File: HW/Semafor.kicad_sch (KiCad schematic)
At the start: 65 parts, among them J1 USB_C_Receptacle_USB2.0, J2 USB_plug, M1 Motor_DC, Q3 Q_NMOS_GSD, Q4 Q_NMOS_GSD, SW6 SW_SPDT, U1 ESP32-C3, U2 CN3058E, U3 LT1930, U4 E22-900T22D, U5 AT42QT1070-S, U6 CJ431

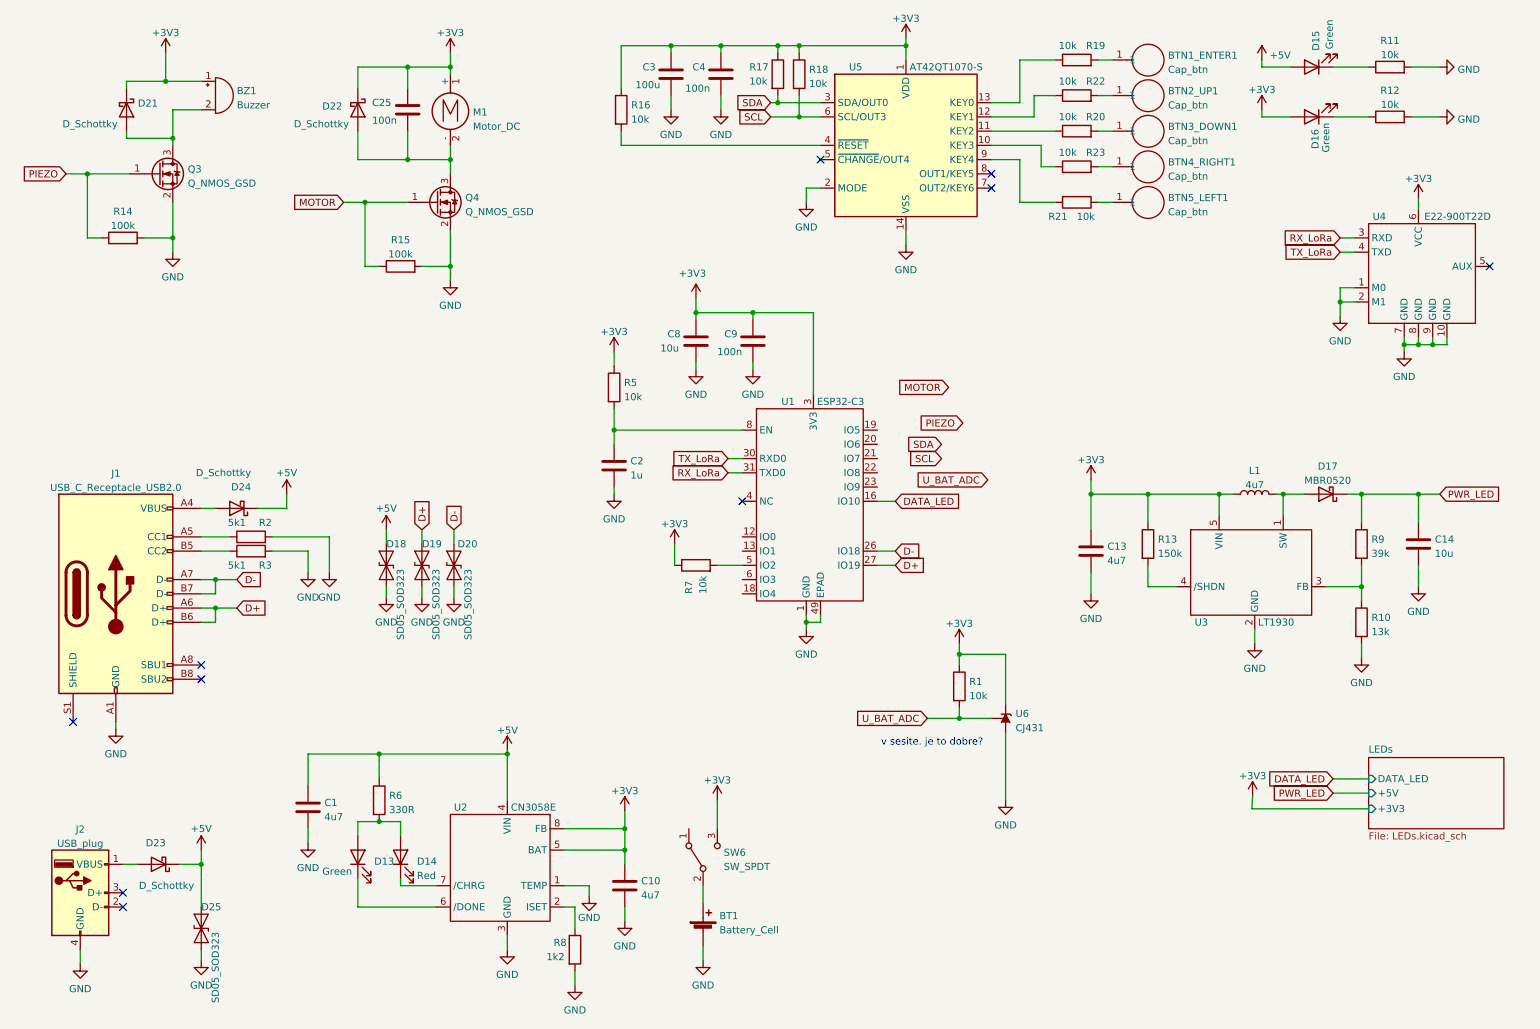
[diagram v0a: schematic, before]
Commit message: repair mistakes in schematic, add switched supply voltage to LoRa, LEDs and converter for capacitive buttons
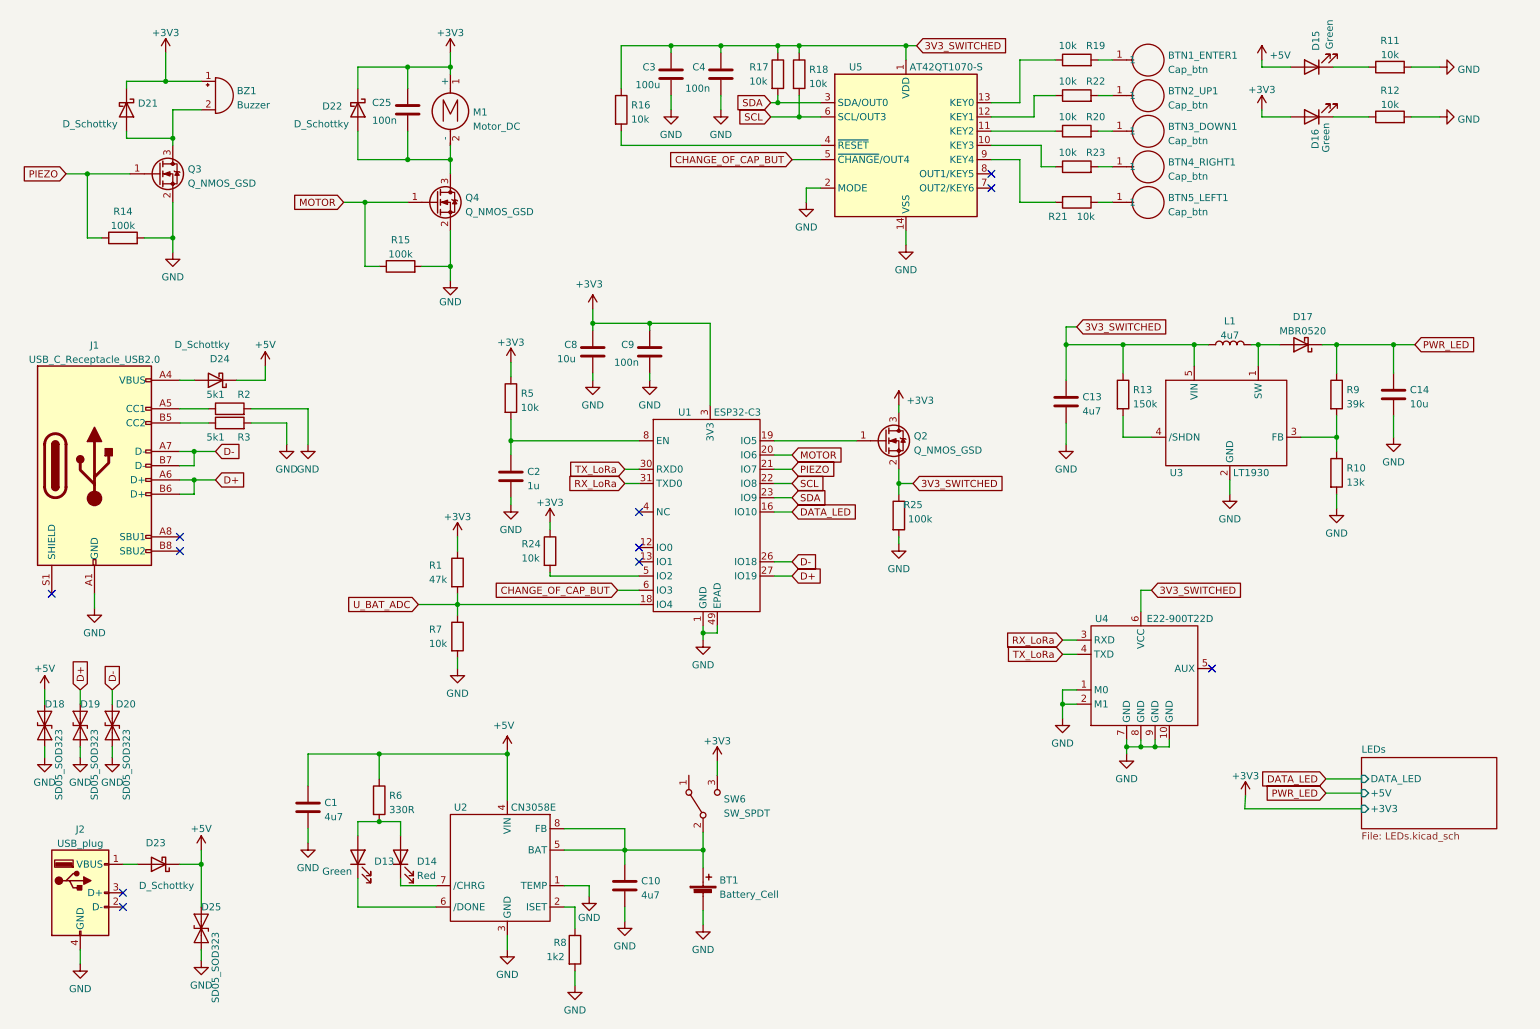
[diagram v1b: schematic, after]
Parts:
- removed U6: CJ431, Package_TO_SOT_SMD:SOT-23, symbol Reference_Voltage:CJ432
- added Q2: Q_NMOS_GSD, Package_TO_SOT_SMD:SOT-23, symbol Device:Q_NMOS_GSD
- added R24: 10k, Resistor_SMD:R_0603_1608Metric, symbol Device:R
- added R25: 100k, Resistor_SMD:R_0603_1608Metric, symbol Device:R
- R1: value 10k -> 47k
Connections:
- net +3V3: now also Q2.3 (D), R24.1; no longer C10.1, C13.1, C3.1, C4.1, L1.1, R13.1, R16.1, R17.1, R18.1, R7.1, U2.5 (BAT), U2.8 (FB), U3.5 (VIN), U4.6 (VCC), U5.1 (VDD)
- net GND: now also R7.2, R25.2
- net MOTOR: now also U1.20 (IO6)
- net PIEZO: now also U1.21 (IO7)
- net SCL: now also U1.22 (IO8)
- net SDA: now also U1.23 (IO9)
- net U_BAT_ADC: now also R7.1, U1.18 (IO4)
- net at U1.5 (IO2): now also R24.2; no longer R7.2
- net at U1.19 (IO5): now also Q2.1 (G)
- net CHANGE_OF_CAP_BUT: now reaches U1.6 (IO3)
- net CHANGE_OF_CAP_BUT: now also U5.5 (~{CHANGE}/OUT4)
- net at BT1.1 (+), SW6.2 (B): now also C10.1, U2.5 (BAT), U2.8 (FB)
- new net 3V3_SWITCHED: C13.1, C3.1, C4.1, L1.1, Q2.2 (S), R13.1, R16.1, R17.1, R18.1, R25.1, U3.5 (VIN), U4.6 (VCC), U5.1 (VDD)
- no-connect marks 10 -> 11
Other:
- note removed: "v sesite. je to dobre?"
- moved on the sheet: BT1, C13, C14, C2, C8, C9, D17, D18, D19, D20, D24, J1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

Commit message: repair ERC errors
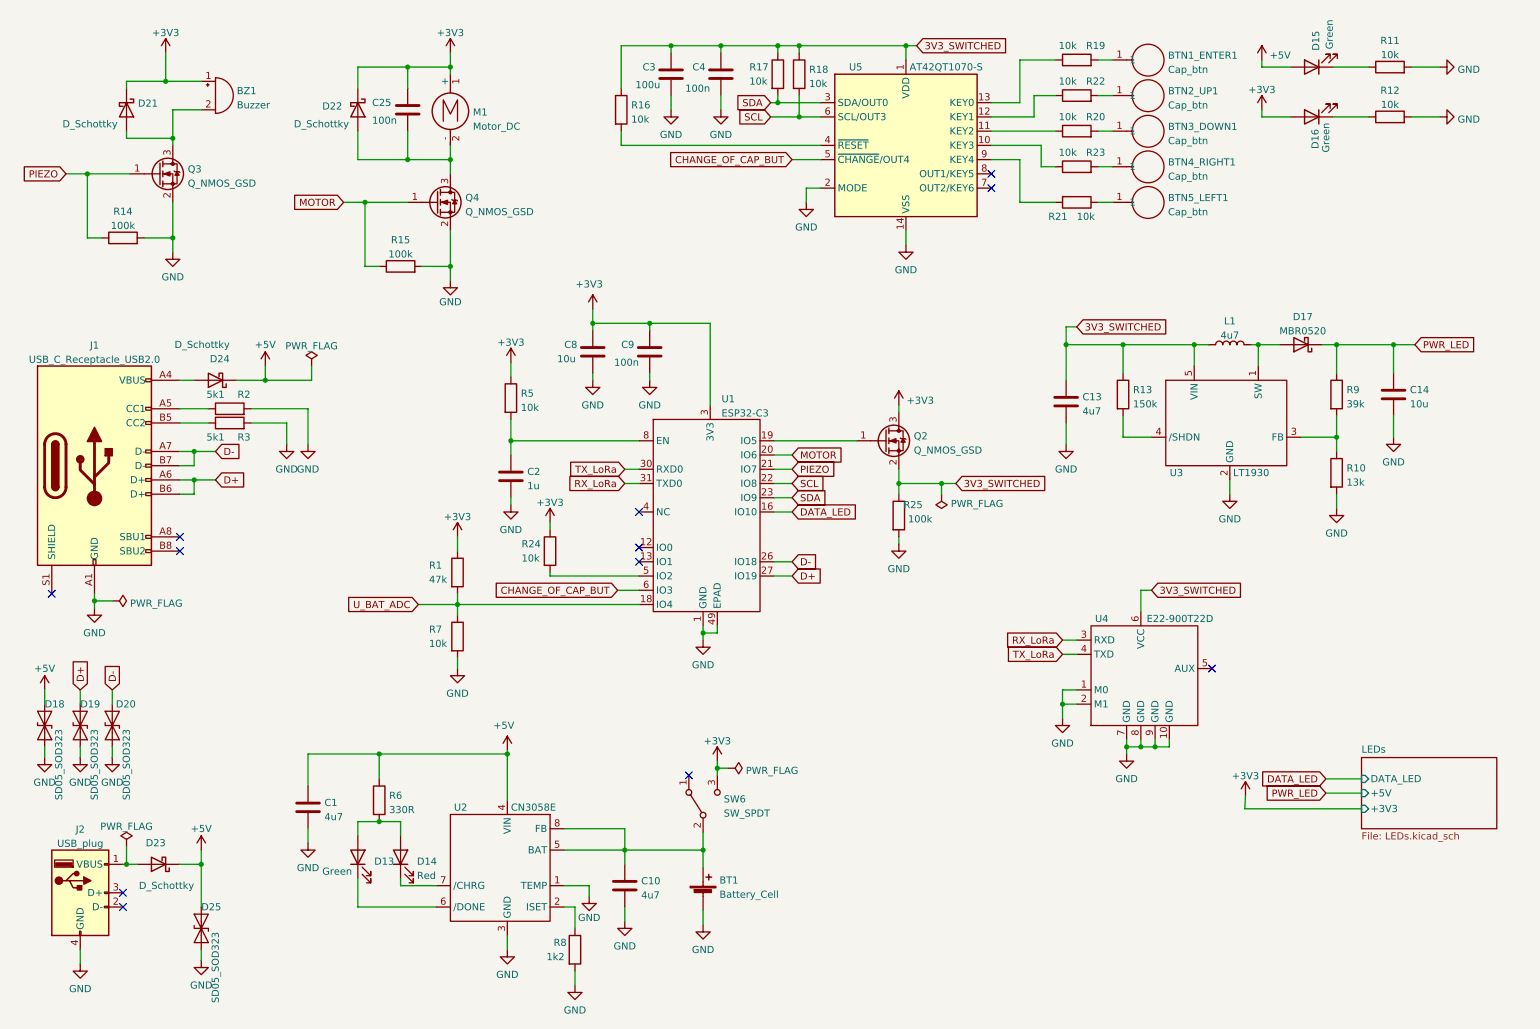
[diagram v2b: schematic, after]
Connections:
- no-connect marks 11 -> 12

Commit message: add some codes for assembly byJLCPCB
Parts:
- BT1, BZ1, C3, U4, U5: LCSC (none) -> ručně
- BTN1_ENTER1, BTN2_UP1, BTN3_DOWN1, BTN4_RIGHT1, BTN5_LEFT1, J2, SW6: LCSC (none) -> -
- C1, C10, C13: LCSC (none) -> C1779
- C14, C8: LCSC (none) -> C15850
- C2: LCSC (none) -> C28323
- C25, C4, C9: LCSC (none) -> C14663
- D13, D15, D16: LCSC (none) -> C965805
- D14: LCSC (none) -> C965799
- J1: LCSC (none) -> C136423
- R1: LCSC (none) -> C25819
- R10: LCSC (none) -> C22797
- R11, R12, R16, R17, R18, R19, R20, R21, R22, R23, R24, R5, R7: LCSC (none) -> C25804
- R13: LCSC (none) -> C22807
- R14, R15, R25: LCSC (none) -> C25803
- R2, R3: LCSC (none) -> C25905
- R6: LCSC (none) -> C23138
- R8: LCSC (none) -> C22765
- R9: LCSC (none) -> C23153
- U1: LCSC (none) -> C2838502
- U2: LCSC (none) -> C112011

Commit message: add LCSC codes for assembly
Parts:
- D18, D19, D20, D25: LCSC (none) -> C3002993
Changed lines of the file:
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@@
+      (effects (font (size 1.27 1.27)) hide)
+    )
+    (property "LCSC" "C3002993" (id 4) (at 32.385 142.875 0)
       (effects (font (size 1.27 1.27)) hide)
     )
@@
       (effects (font (size 1.27 1.27)) hide)
     )
+    (property "LCSC" "C3002993" (id 4) (at 20.32 142.875 0)
+      (effects (font (size 1.27 1.27)) hide)
+    )
     (pin "1")
     (pin "2")
@@
       (effects (font (size 1.27 1.27)) hide)
     )
+    (property "LCSC" "C3002993" (id 4) (at 48.26 179.07 0)
+      (effects (font (size 1.27 1.27)) hide)
+    )
     (pin "1")
     (pin "2")
@@
       (effects (font (size 1.27 1.27)) hide)
     )
+    (property "LCSC" "C3002993" (id 4) (at 26.67 142.875 0)
+      (effects (font (size 1.27 1.27)) hide)
+    )

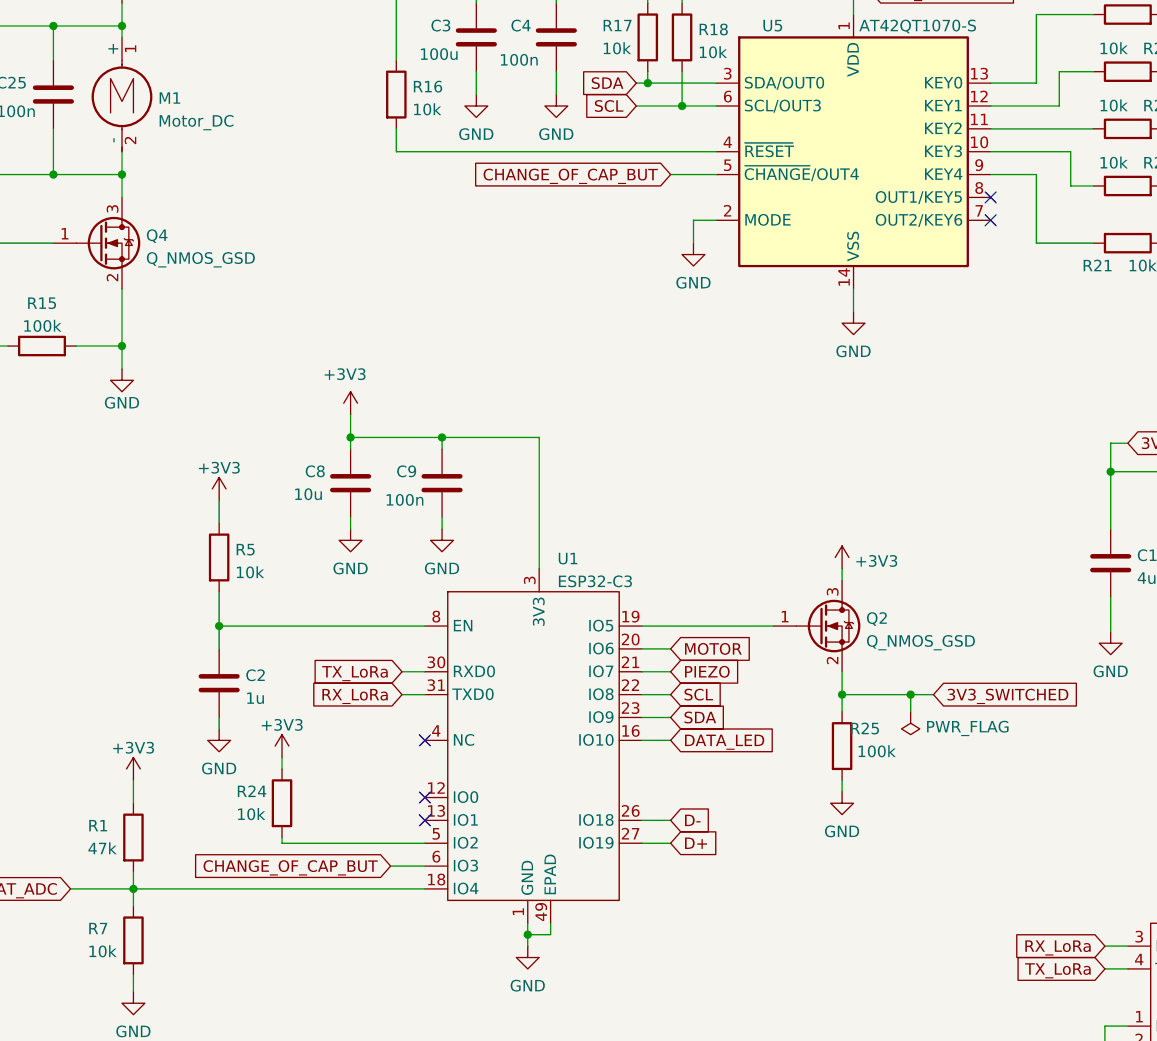
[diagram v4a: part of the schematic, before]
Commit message: repair mistakes from prototype PCB
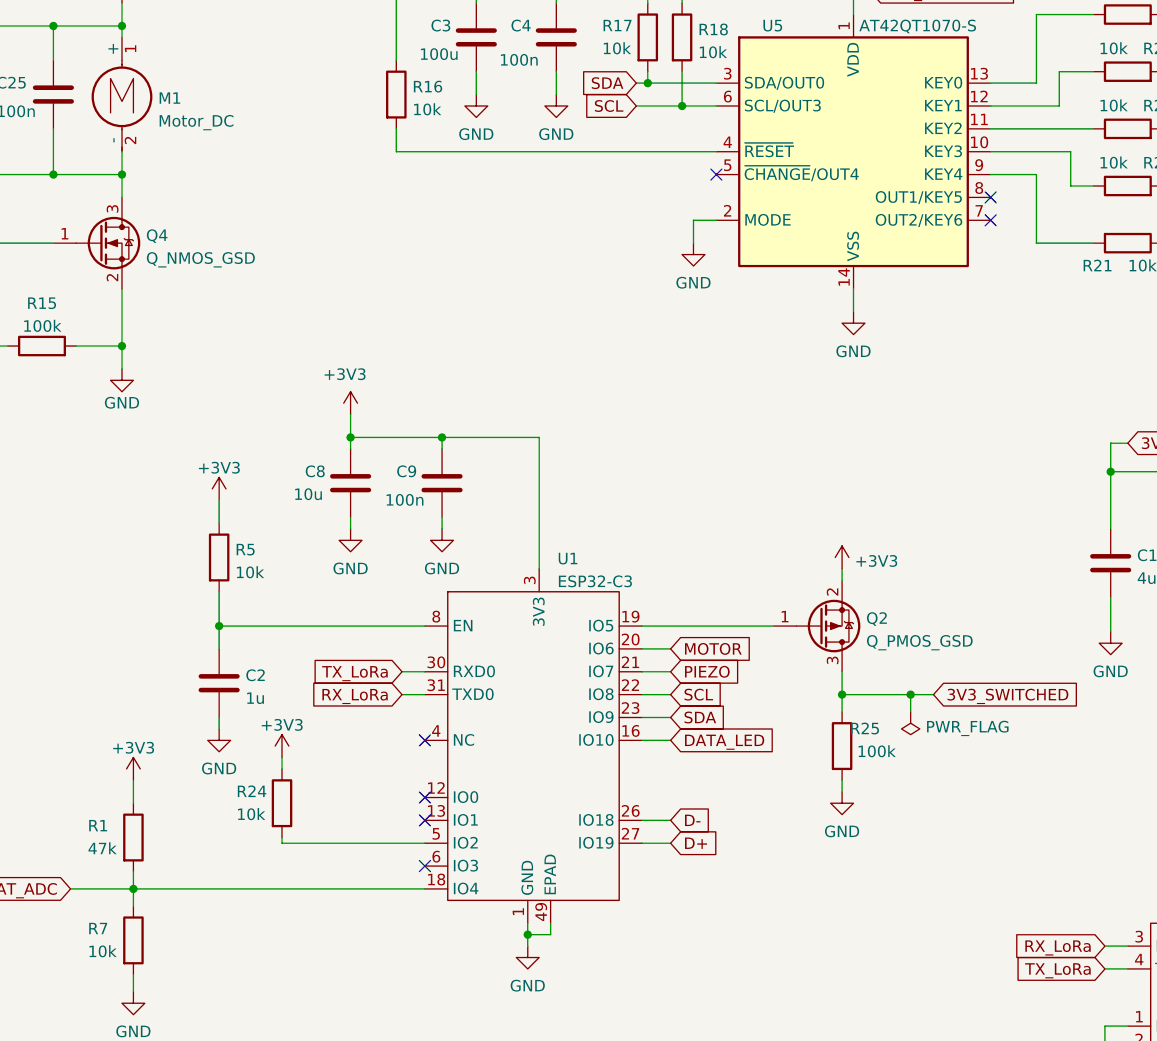
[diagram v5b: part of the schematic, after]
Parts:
- removed Q2: Q_NMOS_GSD, Package_TO_SOT_SMD:SOT-23, symbol Device:Q_NMOS_GSD
- added Q2: Q_PMOS_GSD, Package_TO_SOT_SMD:SOT-23, symbol Device:Q_PMOS_GSD
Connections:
- net +3V3: now also Q2.2 (S)
- net 3V3_SWITCHED: now also Q2.3 (D)
- net at U1.19 (IO5): now also Q2.1 (G)
- net CHANGE_OF_CAP_BUT: no longer names the net of U1.6 (IO3)
- net CHANGE_OF_CAP_BUT: no longer U5.5 (~{CHANGE}/OUT4)
- no-connect marks 12 -> 14
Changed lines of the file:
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@@
   (junction (at 137.795 165.1) (diameter 0) (color 0 0 0 0)
   )
+  (no_connect (at 126.365 118.745))
+  (no_connect (at 158.75 41.91))
   (no_connect (at 126.365 113.665))
   (no_connect (at 34.29 172.72))
@@
     (stroke (width 0) (type default) (color 0 0 0 0))
   )
-  (wire (pts (xy 153.67 41.91) (xy 158.75 41.91))
-    (stroke (width 0) (type default) (color 0 0 0 0))
-  )
   (wire (pts (xy 208.28 30.48) (xy 210.82 30.48))
     (stroke (width 0) (type default) (color 0 0 0 0))
@@
     (stroke (width 0) (type default) (color 0 0 0 0))
   )
-  (wire (pts (xy 122.555 118.745) (xy 126.365 118.745))
-    (stroke (width 0) (type default) (color 0 0 0 0))
-  )
   (wire (pts (xy 151.13 31.75) (xy 158.75 31.75))
     (stroke (width 0) (type default) (color 0 0 0 0))
@@
     )
   )
-  (global_label "CHANGE_OF_CAP_BUT" (shape input) (at 153.67 41.91 180) (fields_autoplaced)
-    (effects (font (size 1.27 1.27)) (justify right))
-    (property "Intersheet References" "${INTERSHEET_REFS}" (id 0) (at 131.2998 41.8306 0)
-      (effects (font (size 1.27 1.27)) (justify right) hide)
-    )
-  )
   (global_label "3V3_SWITCHED" (shape input) (at 204.47 71.755 0) (fields_autoplaced)
     (effects (font (size 1.27 1.27)) (justify left))
@@
     )
   )
-  (global_label "CHANGE_OF_CAP_BUT" (shape input) (at 122.555 118.745 180) (fields_autoplaced)
-    (effects (font (size 1.27 1.27)) (justify right))
-    (property "Intersheet References" "${INTERSHEET_REFS}" (id 0) (at 100.1848 118.6656 0)
-      (effects (font (size 1.27 1.27)) (justify right) hide)
-    )
-  )
   (global_label "PIEZO" (shape input) (at 24.13 44.45 180) (fields_autoplaced)
     (effects (font (size 1.27 1.27)) (justify right))
@@
     (pin "2")
   )
+  (symbol (lib_id "Device:Q_PMOS_GSD") (at 170.18 92.075 0) (mirror x) (unit 1)
+    (in_bom yes) (on_board yes) (fields_autoplaced)
+    (property "Reference" "Q2" (id 0) (at 175.387 91.2403 0)
+      (effects (font (size 1.27 1.27)) (justify left))
+    )
+    (property "Value" "Q_PMOS_GSD" (id 1) (at 175.387 93.7772 0)
+      (effects (font (size 1.27 1.27)) (justify left))
+    )
+    (property "Footprint" "Package_TO_SOT_SMD:SOT-23" (id 2) (at 175.26 94.615 0)
+      (effects (font (size 1.27 1.27)) hide)
+    )
+    (property "Datasheet" "~" (id 3) (at 170.18 92.075 0)
+      (effects (font (size 1.27 1.27)) hide)
+    )
+    (property "LCSC" "C10487" (id 4) (at 170.18 92.075 0)
+      (effects (font (size 1.27 1.27)) hide)
+    )
+    (pin "1")
+    (pin "2")
+    (pin "3")
+  )
   (symbol (lib_id "Library:CN3058E") (at 102.87 168.91 0) (unit 1)
     (in_bom yes) (on_board yes)
@@
     (pin "1")
   )
-  (symbol (lib_id "Device:Q_NMOS_GSD") (at 170.18 92.075 0) (unit 1)
-    (in_bom yes) (on_board yes) (fields_autoplaced)
-    (property "Reference" "Q2" (id 0) (at 175.387 91.2403 0)
-      (effects (font (size 1.27 1.27)) (justify left))
-    )
-    (property "Value" "Q_NMOS_GSD" (id 1) (at 175.387 93.7772 0)
-      (effects (font (size 1.27 1.27)) (justify left))
-    )
-    (property "Footprint" "Package_TO_SOT_SMD:SOT-23" (id 2) (at 175.26 89.535 0)
-      (effects (font (size 1.27 1.27)) hide)
-    )
-    (property "Datasheet" "~" (id 3) (at 170.18 92.075 0)
-      (effects (font (size 1.27 1.27)) hide)
-    )
-    (property "LCSC" "C8545" (id 4) (at 170.18 92.075 0)
-      (effects (font (size 1.27 1.27)) hide)
-    )
-    (pin "1")
-    (pin "2")
-    (pin "3")
-  )
   (symbol (lib_id "Device:R") (at 212.725 83.82 0) (unit 1)
     (in_bom yes) (on_board yes) (fields_autoplaced)
@@
       (reference "Q1") (unit 1) (value "Q_NMOS_GSD") (footprint "Package_TO_SOT_SMD:SOT-23")
     )
-    (path "/8c2d0ac6-6dec-459a-b3ca-5b77b79ef2f4"
-      (reference "Q2") (unit 1) (value "Q_NMOS_GSD") (footprint "Package_TO_SOT_SMD:SOT-23")
+    (path "/7e657a2d-a4b9-4673-a751-0ef571dac198"
+      (reference "Q2") (unit 1) (value "Q_PMOS_GSD") (footprint "Package_TO_SOT_SMD:SOT-23")
     )
     (path "/b92848c7-8db4-4d0c-a431-1aa9c3862ea8"
